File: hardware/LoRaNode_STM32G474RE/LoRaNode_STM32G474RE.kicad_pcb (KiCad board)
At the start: 2 copper layers, 69.5 x 112.2 mm, 59 parts, among them J1 Conn_01x04_Pin, J2 Conn_01x05_Pin, J3 USB_C_Receptacle_USB2.0_16P, J4 Conn_01x02, J5 Conn_Coaxial, SW1 MSK12C02, U2 AMS1117-3.3, U3 RFM95W-868S2, U4 STM32G474RETx, Y2 24mHz 8pf

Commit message: feat: complete hardware v1 (ERC almost clean) and initial firmware peripherals config
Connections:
- J1 pad 3: /SSD1306{I2C}/SSD1306.SCL -> /I2C1{SCL SDA}/I2C1.SCL
- J1 pad 4: /SSD1306{I2C}/SSD1306.SDA -> /I2C1{SCL SDA}/I2C1.SDA
- U3 pad 14: unconnected-(U3-DIO0-Pad14) -> /STM32/RFM95.DIO0
- U3 pad 2: unconnected-(U3-MISO-Pad2) -> /STM32/RFM95.MISO
- U3 pad 3: unconnected-(U3-MOSI-Pad3) -> /STM32/RFM95.MOSI
- U3 pad 4: unconnected-(U3-SCK-Pad4) -> /STM32/RFM95.SCK
- U3 pad 5: unconnected-(U3-NSS-Pad5) -> /STM32/RFM95.NSS
- U3 pad 6: unconnected-(U3-RESET-Pad6) -> /STM32/RFM95.RST
- U4 pad 51: unconnected-(U4-PA15-Pad51) -> /I2C1{SCL SDA}/I2C1.SDA
- U4 pad 60: unconnected-(U4-PB7-Pad60) -> /I2C1{SCL SDA}/I2C1.SCL
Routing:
- net Net-(J3-CC1): track 8.73 -> 10.2 mm
- net unconnected-(J3-SBU2-PadB8): track 1.49 -> 0.00 mm

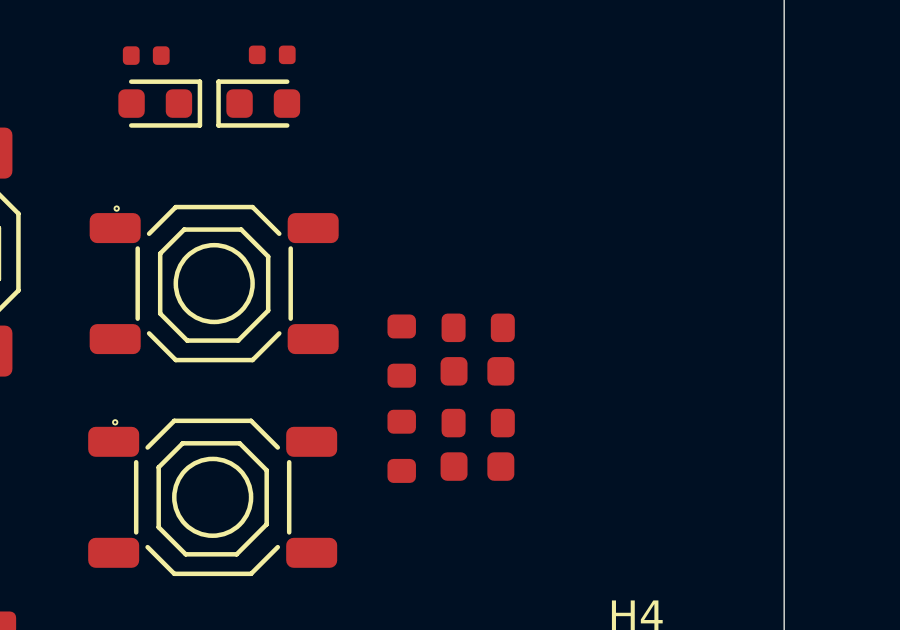
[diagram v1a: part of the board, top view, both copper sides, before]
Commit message: feat: add RFM95W 3D model for hardware and initial FreeRTOS task skeleton for firmware
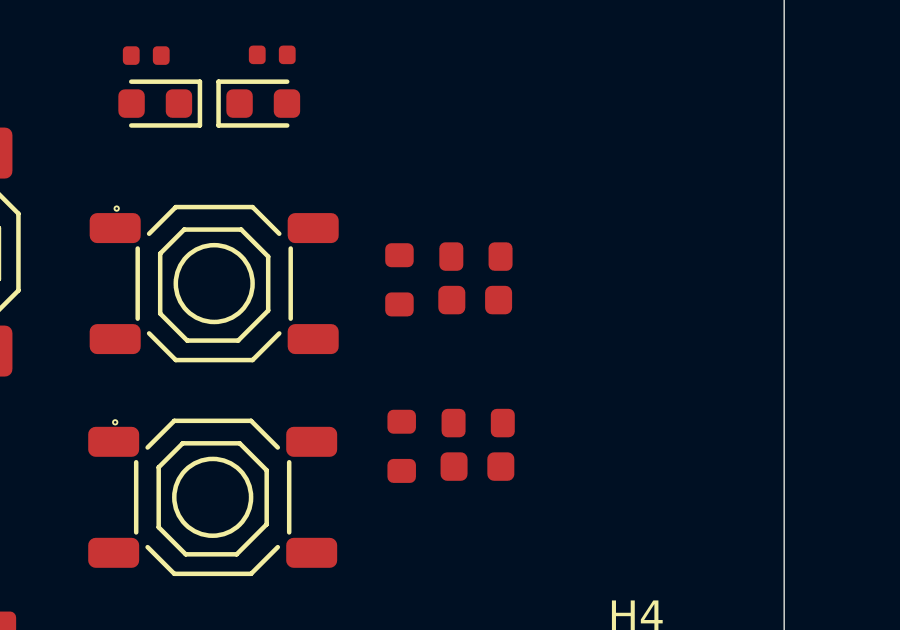
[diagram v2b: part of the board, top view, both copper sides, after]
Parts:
- moved C16 2.38 mm to (166.4, 122.0)
- moved R16 2.38 mm to (166.5, 120.5)
- moved R15 2.38 mm to (163.9, 121.3)
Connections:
- R20 pad 2: /STM32/SSD1306.SDA -> /I2C1{SCL SDA}/I2C1.SDA
- R22 pad 2: /STM32/SSD1306.SCL -> /I2C1{SCL SDA}/I2C1.SCL
